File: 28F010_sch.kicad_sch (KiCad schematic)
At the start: 13 parts, among them U10 74LVC1G332, U11 74LS138, U12 CY7C199, U15 CY7C199, U16 4012, U17 CY7C199, U3 74LS04, U8 74LS138, U9 CY7C199

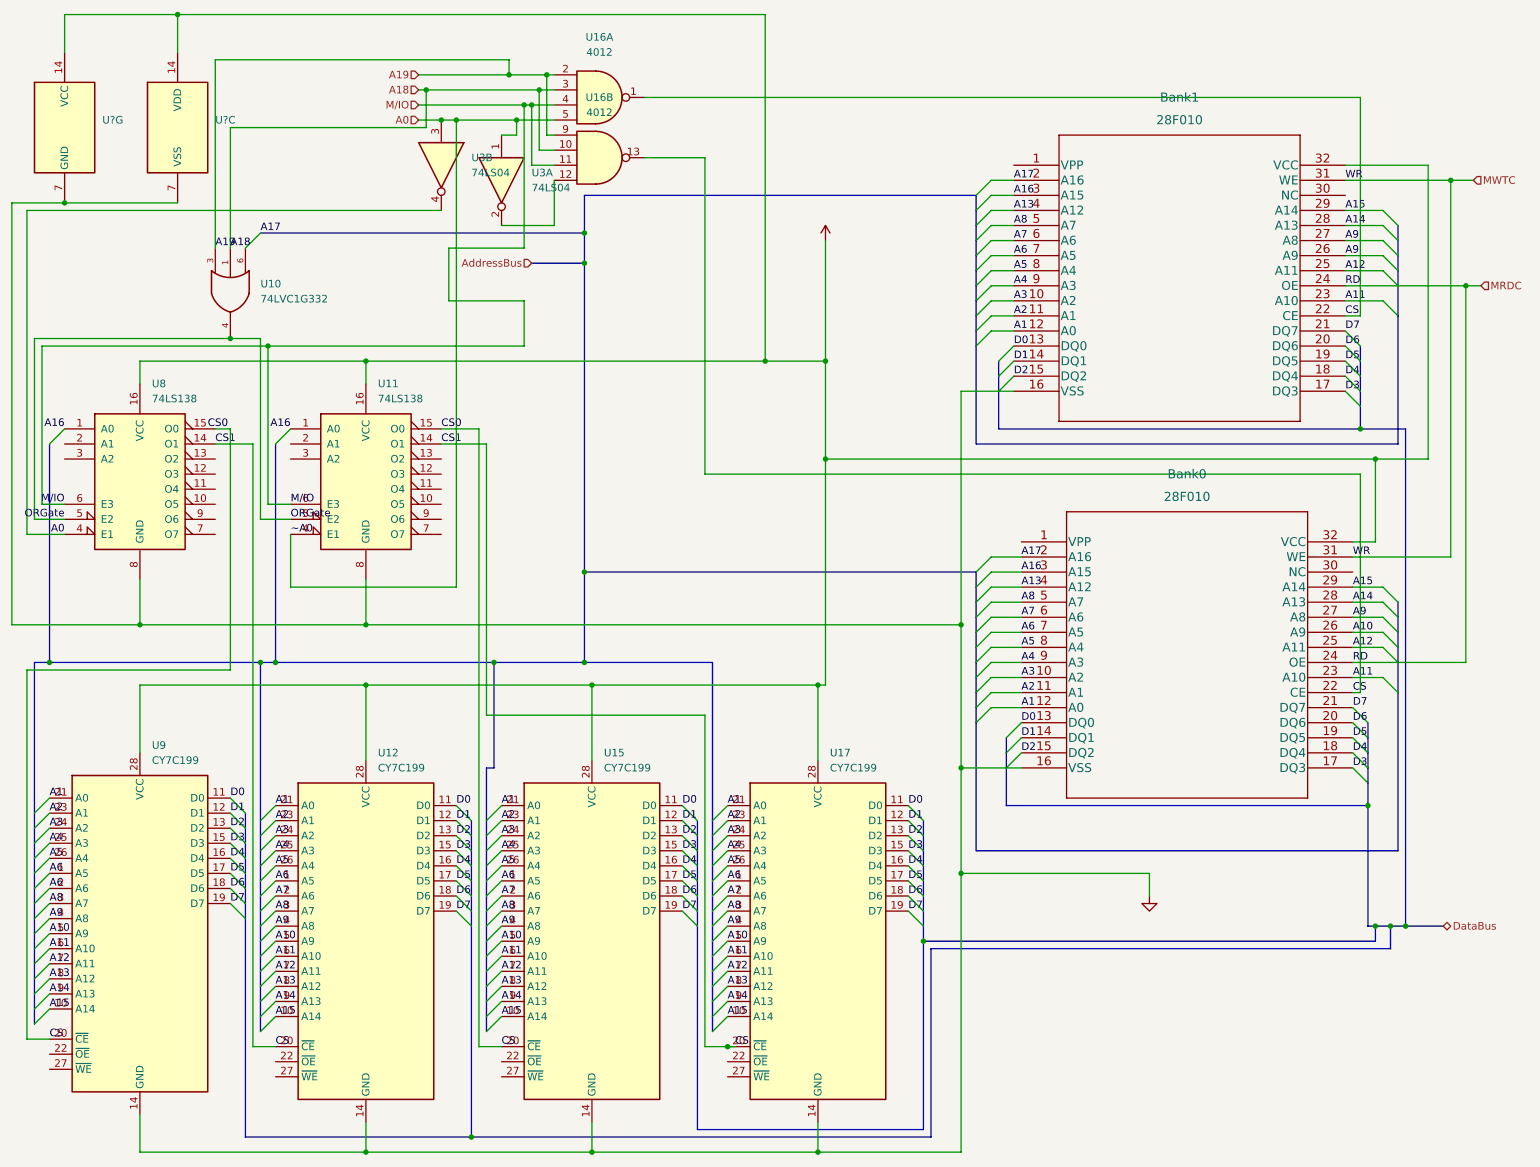
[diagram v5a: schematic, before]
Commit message: Enabled inputs on the max235
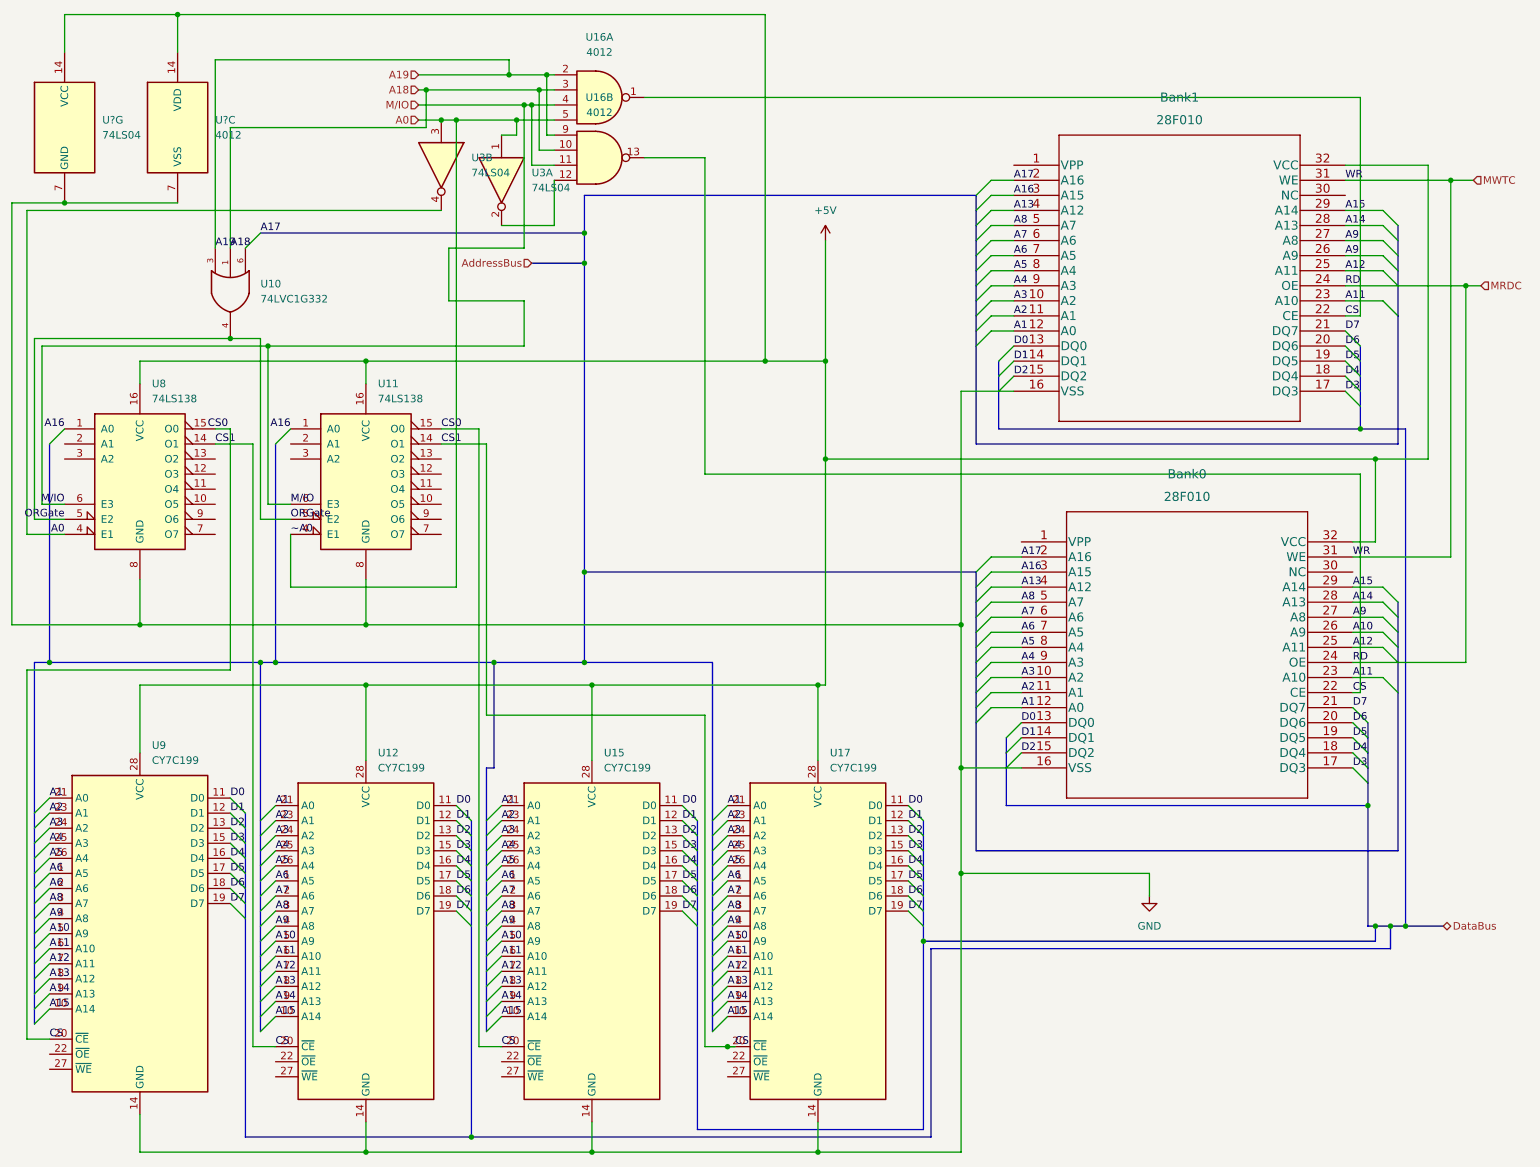
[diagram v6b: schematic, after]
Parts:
- U?: value (none) -> 74LS04
- U?: value (none) -> 4012
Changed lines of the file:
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@@
       (effects (font (size 1.27 1.27)) hide)
     )
-    (property "Value" "" (id 1) (at 149.86 38.1 0))
+    (property "Value" "+5V" (id 1) (at 149.86 38.1 0))
     (property "Footprint" "" (id 2) (at 149.86 43.18 0)
       (effects (font (size 1.27 1.27)) hide)
@@
       (effects (font (size 1.27 1.27)) (justify left))
     )
-    (property "Value" "" (id 1) (at 27.94 25.3999 0)
+    (property "Value" "74LS04" (id 1) (at 27.94 25.3999 0)
       (effects (font (size 1.27 1.27)) (justify left))
     )
@@
       (effects (font (size 1.27 1.27)) hide)
     )
-    (property "Value" "" (id 1) (at 204.47 158.75 0))
+    (property "Value" "GND" (id 1) (at 204.47 158.75 0))
     (property "Footprint" "" (id 2) (at 204.47 153.67 0)
       (effects (font (size 1.27 1.27)) hide)
@@
       (effects (font (size 1.27 1.27)) (justify left))
     )
-    (property "Value" "" (id 1) (at 46.99 25.3999 0)
-      (effects (font (size 1.27 1.27)) (justify left))
-    )
+    (property "Value" "4012" (id 1) (at 46.99 25.3999 0)
+      (effects (font (size 1.27 1.27)) (justify left))
+    )

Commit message: Updated PCB
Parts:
- Bank0, Bank1: value 28F010 -> (none); footprint parts:28F010 -> (none)
- U10: value 74LVC1G332 -> (none); footprint Package_TO_SOT_SMD:SOT-23-6 -> (none)
- U11, U8: value 74LS138 -> (none); footprint Package_DIP:DIP-16_W7.62mm -> (none)
- U12, U15, U17, U9: value CY7C199 -> (none); footprint Package_DIP:DIP-28_W7.62mm -> (none)
- U16: value 4012 -> (none); footprint Package_DIP:DIP-12_W7.62mm -> (none)
- U3: value 74LS04 -> (none); footprint Package_DIP:DIP-14_W7.62mm -> (none)
- U39: renamed from U?; value 74LS04 -> (none)
- U40: renamed from U?; value 4012 -> (none)
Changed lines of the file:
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@@
       (effects (font (size 1.27 1.27)) (justify left))
     )
-    (property "Value" "74LS04" (id 1) (at 90.17 31.7499 90)
-      (effects (font (size 1.27 1.27)) (justify left))
-    )
-    (property "Footprint" "Package_DIP:DIP-14_W7.62mm" (id 2) (at 85.09 30.48 0)
+    (property "Value" "" (id 1) (at 90.17 31.7499 90)
+      (effects (font (size 1.27 1.27)) (justify left))
+    )
+    (property "Footprint" "" (id 2) (at 85.09 30.48 0)
       (effects (font (size 1.27 1.27)) hide)
     )
@@
       (effects (font (size 1.524 1.524)))
     )
-    (property "Value" "28F010" (id 1) (at 210.82 86.36 0)
+    (property "Value" "" (id 1) (at 210.82 86.36 0)
       (effects (font (size 1.524 1.524)))
     )
-    (property "Footprint" "parts:28F010" (id 2) (at 210.82 87.884 0)
+    (property "Footprint" "" (id 2) (at 210.82 87.884 0)
       (effects (font (size 1.524 1.524)) hide)
     )
@@
   (symbol (lib_id "power:+5V") (at 149.86 43.18 0) (unit 1)
     (in_bom yes) (on_board yes) (fields_autoplaced)
-    (property "Reference" "#PWR?" (id 0) (at 149.86 46.99 0)
+    (property "Reference" "#PWR0123" (id 0) (at 149.86 46.99 0)
       (effects (font (size 1.27 1.27)) hide)
     )
@@
   (symbol (lib_id "74xx:74LS04") (at 21.59 24.13 0) (unit 7)
     (in_bom yes) (on_board yes) (fields_autoplaced)
-    (property "Reference" "U?" (id 0) (at 27.94 22.8599 0)
-      (effects (font (size 1.27 1.27)) (justify left))
-    )
-    (property "Value" "74LS04" (id 1) (at 27.94 25.3999 0)
+    (property "Reference" "U39" (id 0) (at 27.94 22.8599 0)
+      (effects (font (size 1.27 1.27)) (justify left))
+    )
+    (property "Value" "" (id 1) (at 27.94 25.3999 0)
       (effects (font (size 1.27 1.27)) (justify left))
     )
@@
       (effects (font (size 1.27 1.27)) (justify left))
     )
-    (property "Value" "74LS138" (id 1) (at 74.4094 69.85 0)
-      (effects (font (size 1.27 1.27)) (justify left))
-    )
-    (property "Footprint" "Package_DIP:DIP-16_W7.62mm" (id 2) (at 72.39 82.55 0)
+    (property "Value" "" (id 1) (at 74.4094 69.85 0)
+      (effects (font (size 1.27 1.27)) (justify left))
+    )
+    (property "Footprint" "" (id 2) (at 72.39 82.55 0)
       (effects (font (size 1.27 1.27)) hide)
     )
@@
   (symbol (lib_id "power:GND") (at 204.47 153.67 0) (unit 1)
     (in_bom yes) (on_board yes) (fields_autoplaced)
-    (property "Reference" "#PWR?" (id 0) (at 204.47 160.02 0)
+    (property "Reference" "#PWR0122" (id 0) (at 204.47 160.02 0)
       (effects (font (size 1.27 1.27)) hide)
     )
@@
       (effects (font (size 1.27 1.27)) (justify left))
     )
-    (property "Value" "CY7C199" (id 1) (at 112.5094 132.08 0)
-      (effects (font (size 1.27 1.27)) (justify left))
-    )
-    (property "Footprint" "Package_DIP:DIP-28_W7.62mm" (id 2) (at 110.49 161.29 0)
+    (property "Value" "" (id 1) (at 112.5094 132.08 0)
+      (effects (font (size 1.27 1.27)) (justify left))
+    )
+    (property "Footprint" "" (id 2) (at 110.49 161.29 0)
       (effects (font (size 1.27 1.27)) hide)
     )
@@
       (effects (font (size 1.27 1.27)) (justify left))
     )
-    (property "Value" "74LS138" (id 1) (at 36.3094 69.85 0)
-      (effects (font (size 1.27 1.27)) (justify left))
-    )
-    (property "Footprint" "Package_DIP:DIP-16_W7.62mm" (id 2) (at 34.29 82.55 0)
+    (property "Value" "" (id 1) (at 36.3094 69.85 0)
+      (effects (font (size 1.27 1.27)) (justify left))
+    )
+    (property "Footprint" "" (id 2) (at 34.29 82.55 0)
       (effects (font (size 1.27 1.27)) hide)
     )
@@
     (in_bom yes) (on_board yes) (fields_autoplaced)
     (property "Reference" "U16" (id 0) (at 111.76 8.89 0))
-    (property "Value" "4012" (id 1) (at 111.76 11.43 0))
-    (property "Footprint" "Package_DIP:DIP-12_W7.62mm" (id 2) (at 111.76 19.05 0)
+    (property "Value" "" (id 1) (at 111.76 11.43 0))
+    (property "Footprint" "" (id 2) (at 111.76 19.05 0)
       (effects (font (size 1.27 1.27)) hide)
     )
@@
       (effects (font (size 1.27 1.27)) (justify left))
     )
-    (property "Value" "74LS04" (id 1) (at 100.33 34.2899 90)
-      (effects (font (size 1.27 1.27)) (justify left))
-    )
-    (property "Footprint" "Package_DIP:DIP-14_W7.62mm" (id 2) (at 95.25 33.02 0)
+    (property "Value" "" (id 1) (at 100.33 34.2899 90)
+      (effects (font (size 1.27 1.27)) (justify left))
+    )
+    (property "Footprint" "" (id 2) (at 95.25 33.02 0)
       (effects (font (size 1.27 1.27)) hide)
     )
@@
       (effects (font (size 1.27 1.27)) (justify left))
     )
-    (property "Value" "CY7C199" (id 1) (at 36.3094 130.81 0)
-      (effects (font (size 1.27 1.27)) (justify left))
-    )
-    (property "Footprint" "Package_DIP:DIP-28_W7.62mm" (id 2) (at 34.29 160.02 0)
+    (property "Value" "" (id 1) (at 36.3094 130.81 0)
+      (effects (font (size 1.27 1.27)) (justify left))
+    )
+    (property "Footprint" "" (id 2) (at 34.29 160.02 0)
       (effects (font (size 1.27 1.27)) hide)
     )
@@
       (effects (font (size 1.27 1.27)) (justify left))
     )
-    (property "Value" "74LVC1G332" (id 1) (at 54.61 53.0224 90)
-      (effects (font (size 1.27 1.27)) (justify left))
-    )
-    (property "Footprint" "Package_TO_SOT_SMD:SOT-23-6" (id 2) (at 49.53 52.07 0)
+    (property "Value" "" (id 1) (at 54.61 53.0224 90)
+      (effects (font (size 1.27 1.27)) (justify left))
+    )
+    (property "Footprint" "" (id 2) (at 49.53 52.07 0)
       (effects (font (size 1.27 1.27)) hide)
     )
@@
       (effects (font (size 1.27 1.27)) (justify left))
     )
-    (property "Value" "CY7C199" (id 1) (at 150.6094 132.08 0)
-      (effects (font (size 1.27 1.27)) (justify left))
-    )
-    (property "Footprint" "Package_DIP:DIP-28_W7.62mm" (id 2) (at 148.59 161.29 0)
+    (property "Value" "" (id 1) (at 150.6094 132.08 0)
+      (effects (font (size 1.27 1.27)) (justify left))
+    )
+    (property "Footprint" "" (id 2) (at 148.59 161.29 0)
       (effects (font (size 1.27 1.27)) hide)
     )
@@
       (effects (font (size 1.524 1.524)))
     )
-    (property "Value" "28F010" (id 1) (at 209.55 22.86 0)
+    (property "Value" "" (id 1) (at 209.55 22.86 0)
       (effects (font (size 1.524 1.524)))
     )
-    (property "Footprint" "parts:28F010" (id 2) (at 209.55 24.384 0)
+    (property "Footprint" "" (id 2) (at 209.55 24.384 0)
       (effects (font (size 1.524 1.524)) hide)
     )
@@
     (in_bom yes) (on_board yes) (fields_autoplaced)
     (property "Reference" "U16" (id 0) (at 111.76 19.05 0))
-    (property "Value" "4012" (id 1) (at 111.76 21.59 0))
-    (property "Footprint" "Package_DIP:DIP-12_W7.62mm" (id 2) (at 111.76 29.21 0)
+    (property "Value" "" (id 1) (at 111.76 21.59 0))
+    (property "Footprint" "" (id 2) (at 111.76 29.21 0)
       (effects (font (size 1.27 1.27)) hide)
     )
@@
   (symbol (lib_id "4xxx:4012") (at 40.64 24.13 0) (unit 3)
     (in_bom yes) (on_board yes) (fields_autoplaced)
-    (property "Reference" "U?" (id 0) (at 46.99 22.8599 0)
-      (effects (font (size 1.27 1.27)) (justify left))
-    )
-    (property "Value" "4012" (id 1) (at 46.99 25.3999 0)
+    (property "Reference" "U40" (id 0) (at 46.99 22.8599 0)
+      (effects (font (size 1.27 1.27)) (justify left))
+    )
+    (property "Value" "" (id 1) (at 46.99 25.3999 0)
       (effects (font (size 1.27 1.27)) (justify left))
     )
@@
       (effects (font (size 1.27 1.27)) (justify left))
     )
-    (property "Value" "CY7C199" (id 1) (at 74.4094 132.08 0)
-      (effects (font (size 1.27 1.27)) (justify left))
-    )
-    (property "Footprint" "Package_DIP:DIP-28_W7.62mm" (id 2) (at 72.39 161.29 0)
-      (effects (font (size 1.27 1.27)) hide)
-    )
+    (property "Value" "" (id 1) (at 74.4094 132.08 0)
+      (effects (font (size 1.27 1.27)) (justify left))
+    )
+    (property "Footprint" "" (id 2) (at 72.39 161.29 0)
+      (effects (font (size 1.27 1.27)) hide)
+    )
